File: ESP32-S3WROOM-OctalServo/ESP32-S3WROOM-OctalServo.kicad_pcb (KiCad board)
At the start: 2 copper layers, 66 x 91.4 mm, 52 parts, among them IC201 USBLC6-2SC6, J101 + 5V Servo -, J102 Servo 1, J103 Servo 2, J104 Servo 3, J105 Servo 4, J106 Servo 5, J107 Servo 6, J108 Servo 7, J109 Servo 8, J201 GCT_USB4105, J301 RJ45, J302 RJ45, SW201 RESET, SW202 BOOT, T301 - 15 in +, T302 - 15 out +, U201 ESP32_S3-DEVKIT, U301 TCAN332DR, U401 AP63203

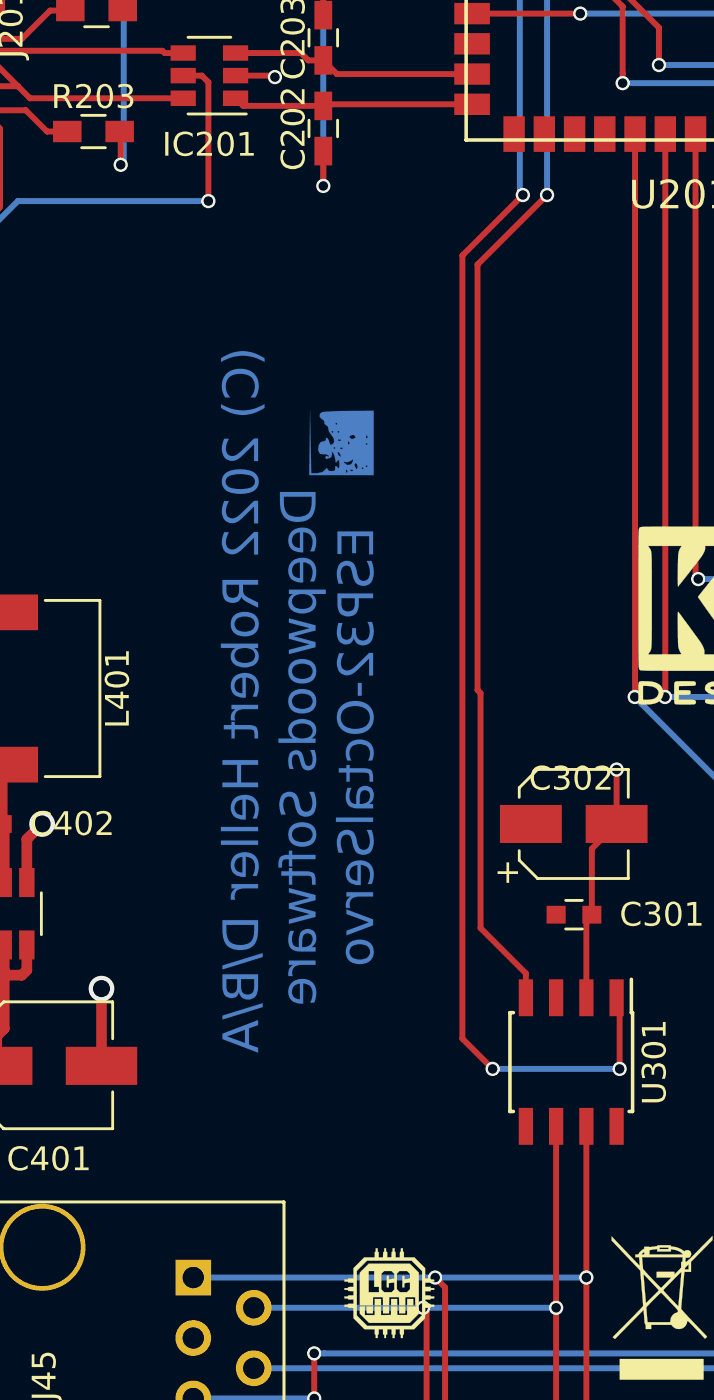
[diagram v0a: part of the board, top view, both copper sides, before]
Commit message: Complete alternitive ESP32 Octal Server boards.
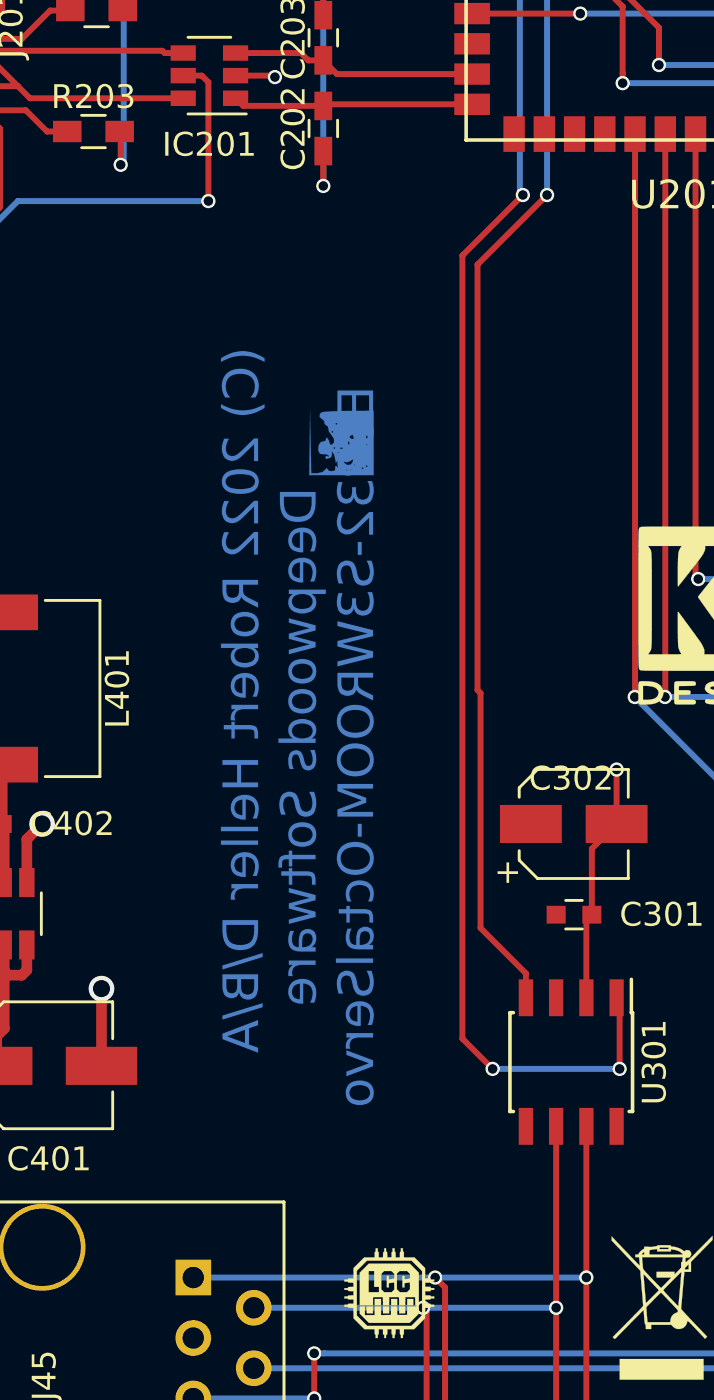
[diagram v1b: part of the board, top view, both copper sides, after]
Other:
- board text added: "(C) 2022 Robert Heller D/B/A Deepwoods Software ESP32-S3WROOM-OctalServo"
- board text removed: "(C) 2022 Robert Heller D/B/A Deepwoods Software ESP32-OctalServo"
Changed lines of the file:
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@@
     (links 117)
     (no_connects 0)
-    (area 10.16 10.16 287.020001 200.660001)
+    (area 144.704999 60.884999 210.895001 152.475001)
     (thickness 1.6)
     (drawings 11)
@@
       (net 63 "Net-(U201-PadEPad)"))
   )
-  (gr_text "(C) 2022 Robert Heller D/B/A \n      Deepwoods Software\n      ESP32-OctalServo" (at 165.735 104.013 90) (layer B.Cu)
+  (gr_text "(C) 2022 Robert Heller D/B/A \n      Deepwoods Software\n      ESP32-S3WROOM-OctalServo" (at 165.735 104.013 90) (layer B.Cu)
     (effects (font (size 1.5 1.5) (thickness 0.3)) (justify mirror))
   )
